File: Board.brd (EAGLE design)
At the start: 47 x 35 mm, 57 parts, among them IC1 CP210X_USB_UART, T1 BC846, T2 BC846

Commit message: cleanup schematic
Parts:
- R1, R2: value (none) -> 470
- R16: value 220k -> 50k
- R17: value 100k -> 220k

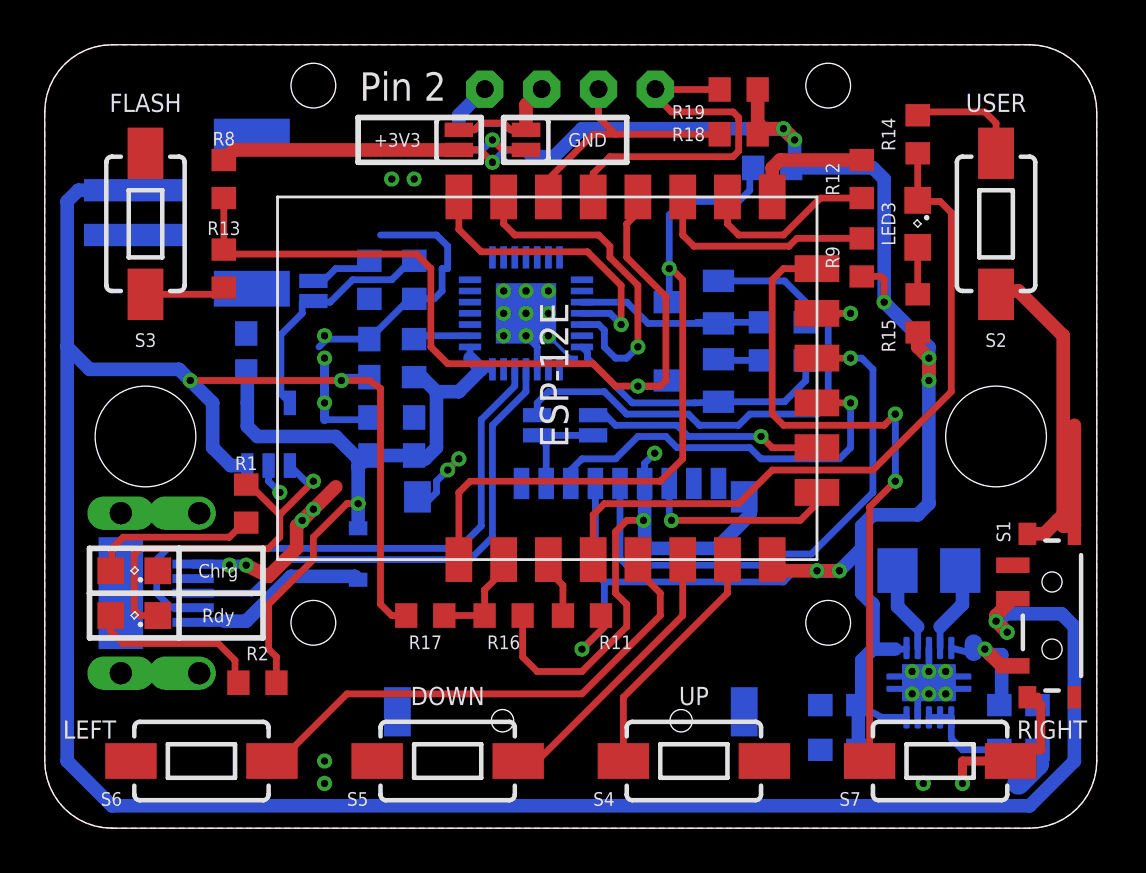
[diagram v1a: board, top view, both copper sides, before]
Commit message: moved pins to new spi out and removed unused components
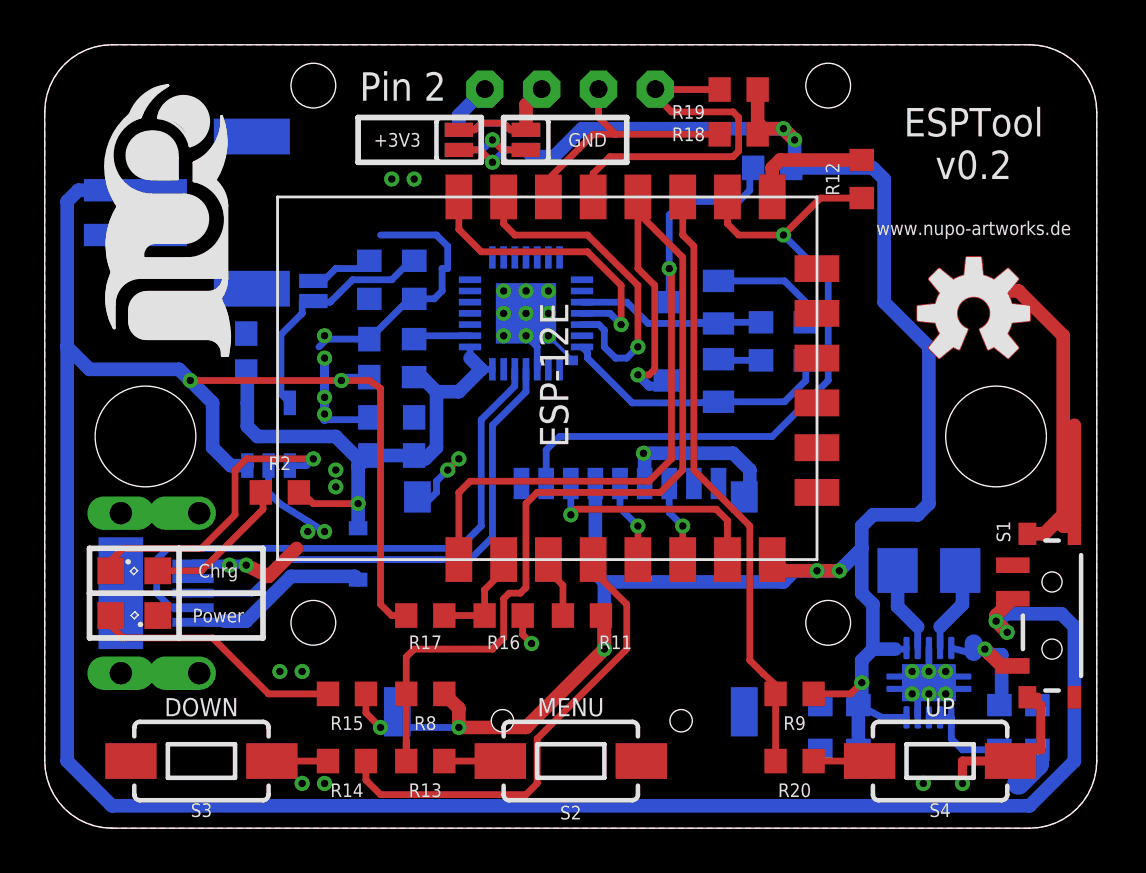
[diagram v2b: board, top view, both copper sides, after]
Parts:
- removed LED2: Charged, led:SML0805
- removed LED3: (no value), led:SML0805
- removed R1: 470, rcl:R0603
- removed S5: DOWN, SparkFun-Electromechanical:TACTILE-SWITCH-1101NE
- removed S6: LEFT, SparkFun-Electromechanical:TACTILE-SWITCH-1101NE
- removed S7: RIGHT, SparkFun-Electromechanical:TACTILE-SWITCH-1101NE
- removed SJ2: HW CS, SparkFun-Retired:SJ_2S-NO
- removed SJ3: SW CS, SparkFun-Retired:SJ_2S-NO
- added POWER: (no value), led:SML0805
- added R20: 470, rcl:R0603
- added U$7: (no value), SparkFun-Aesthetics:OSHW-LOGO-M
- added U$8: (no value), SparkFun-Aesthetics:OSHW-LOGO-M_COPPER
- R15: value 470 -> 1k
- S2: value USER -> FLASH
- S3: value FLASH -> USER
- S4: value UP -> RIGHT
- moved R14 37.9 mm to (13.5, 3.00), turned to 180 degrees
- moved U$5 35.5 mm to (6.50, 27.0), flipped to the top
- moved R15 30.6 mm to (13.5, 6.00), turned to 180 degrees
- moved S2 30.6 mm to (23.5, 3.00), turned to 180 degrees
- moved R8 24.7 mm to (17.0, 6.00), turned to 180 degrees
- moved S3 24.1 mm to (7.00, 3.00), turned to 0 degrees
- moved R13 23.8 mm to (17.0, 3.00), turned to 0 degrees
- moved R9 19.7 mm to (33.5, 6.00), turned to 180 degrees
- moved S4 11.0 mm to (40.0, 3.00), turned to 180 degrees
- moved R2 8.56 mm to (10.5, 15.0)
- moved LED1 2.00 mm to (4.00, 11.5), turned to 0 degrees
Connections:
- removed net GPIO10: MDL1.20, S7.1
- removed net GPIO12: MDL1.6, S5.1
- removed net GPIO13: MDL1.7, S4.1
- removed net GPIO14: MDL1.5, S6.1
- removed net N$11: MDL1.11, R9.2
- removed net N$20: MDL1.10, R12.2
- removed net N$23: MDL1.17, SJ2.2
- removed net N$25: MDL1.19, SJ3.2
- removed net N$9: LED2.A, R1.1
- new net GPIO2: MDL1.11, R20.1, R9.2
- new net N$29: R20.2, S4.2
- net CS: now also MDL1.10, R12.2; no longer SJ2.1, SJ3.1
- net GND: now also POWER.C, S4.1; no longer LED2.C, S4.2, S5.2, S6.2, S7.2
- net GPIO16: no longer LED3.C
- net MISO: now also MDL1.6; no longer MDL1.18
- net MOSI: now also MDL1.7; no longer MDL1.21
- net N$10: no longer R1.2
- net N$21: now also S3.2; no longer S2.2
- net N$22: now also S2.2; no longer S3.2
- net N$24: now also POWER.A; no longer LED3.A
- net SCK: now also MDL1.5; no longer MDL1.22
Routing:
- net GPIO10: track 30.1 -> 0.00 mm, vias 2 -> 0
- net GPIO2: track 0.00 -> 26.9 mm
- net CS: track 4.82 -> 30.8 mm, vias 0 -> 1
- net GPIO14: track 22.9 -> 0.00 mm
- net N$23: track 21.0 -> 0.00 mm, vias 1 -> 0
- net SCK: track 24.3 -> 3.73 mm
- net GND: track 98.2 -> 82.5 mm, vias 34 -> 38
- net GPIO12: track 12.5 -> 0.00 mm
- net GPIO13: track 10.9 -> 0.00 mm
- net GPIO16: track 32.1 -> 21.3 mm
- net N$25: track 10.6 -> 0.00 mm, vias 1 -> 0
- net GPIO0: track 37.4 -> 47.5 mm
- net N$11: track 10.1 -> 0.00 mm
- net N$24: track 2.10 -> 11.4 mm
- net N$20: track 8.09 -> 0.00 mm
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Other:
- board text added: "ESPTool v0.2"
- board text added: "MENU"
- board text added: "Power"
- board text added: "www.nupo-artworks.de"
- board text removed: "FLASH"
- board text removed: "HW CS"
- board text removed: "LEFT"
- board text removed: "RIGHT"
- board text removed: "Rdy"
- board text removed: "SW CS"
- board text removed: "USER"

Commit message: cleanup
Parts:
- moved R2 1.12 mm to (9.50, 14.5), turned to 90 degrees
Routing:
- net GND: track 82.5 -> 68.1 mm, vias 38 -> 36
- net TX0: track 13.4 -> 8.69 mm
- net +3V3: track 101.5 -> 104.5 mm
- net N$7: track 7.40 -> 5.34 mm
- net +5V: track 26.1 -> 27.8 mm
- net NRST: track 30.7 -> 32.1 mm
